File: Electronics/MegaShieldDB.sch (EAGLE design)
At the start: 40 parts, among them IC2 MCP4802, IC3 MCP4802, IC4 4013N, Q1 BF199, Q5 BF199, X1 M25-HD-20, X2 Brake, X4 Cruise Computers, X5 Steer, X6 Motor Controller

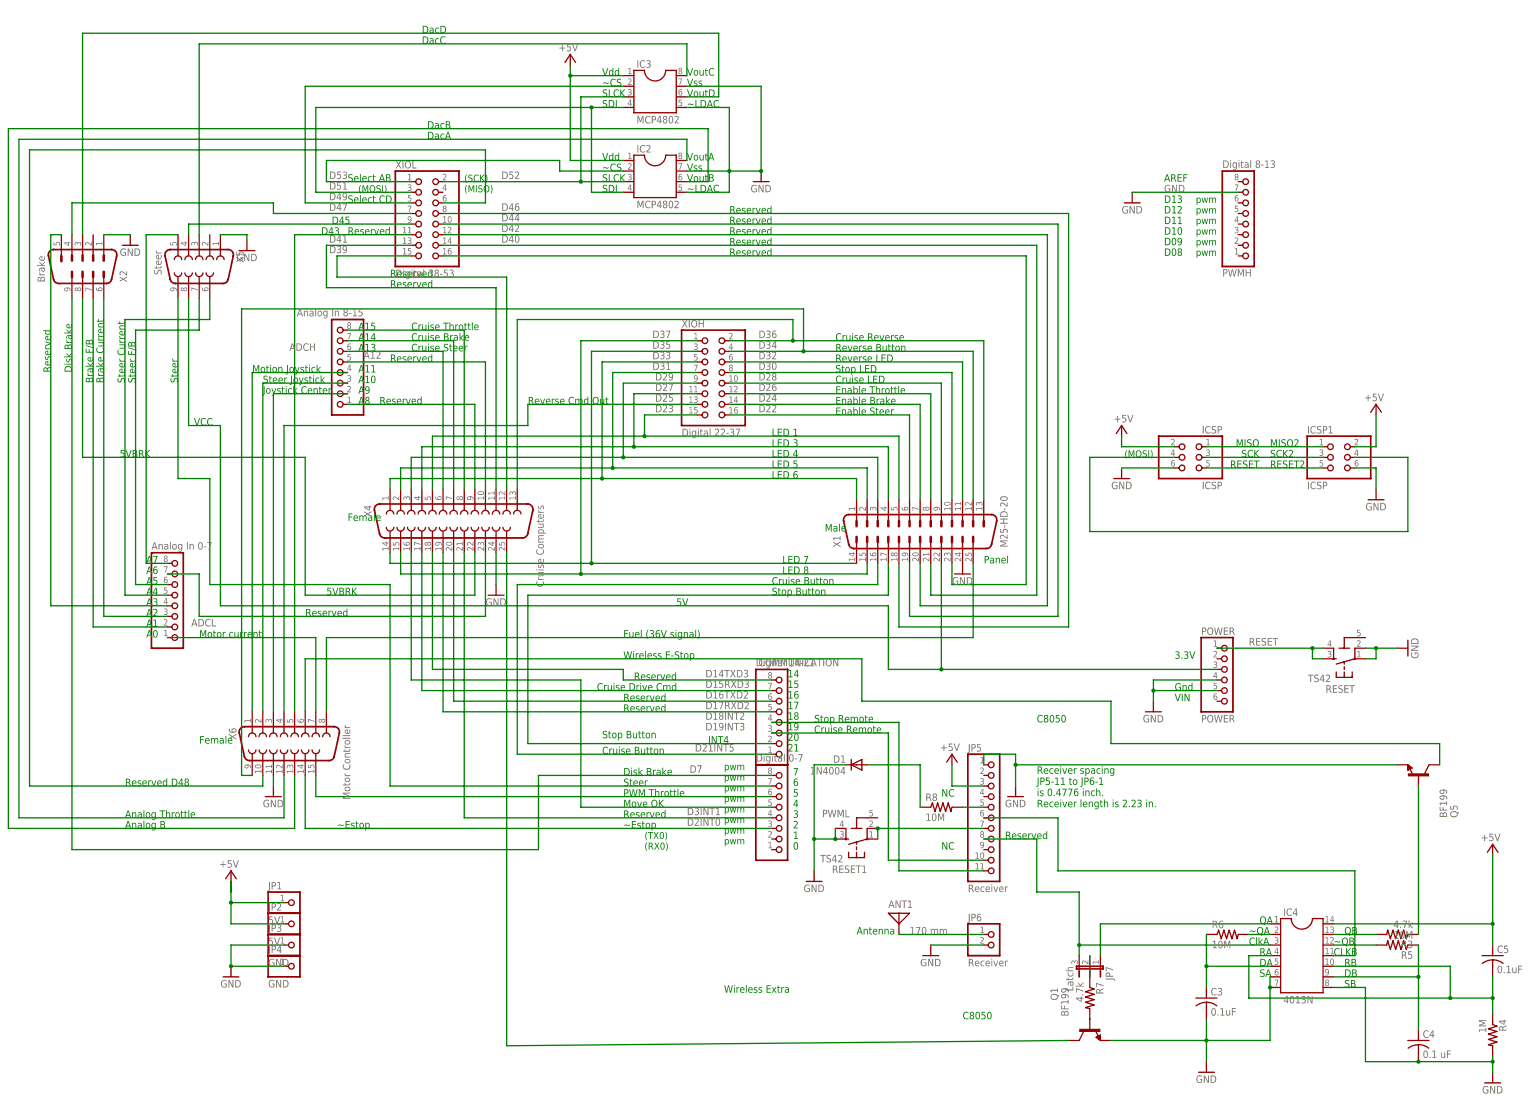
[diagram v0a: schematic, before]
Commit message: Included holes for mounting Mega, board cutouts, renamed connectors. Signals to front panel have been swapped.  Connector names have changed.
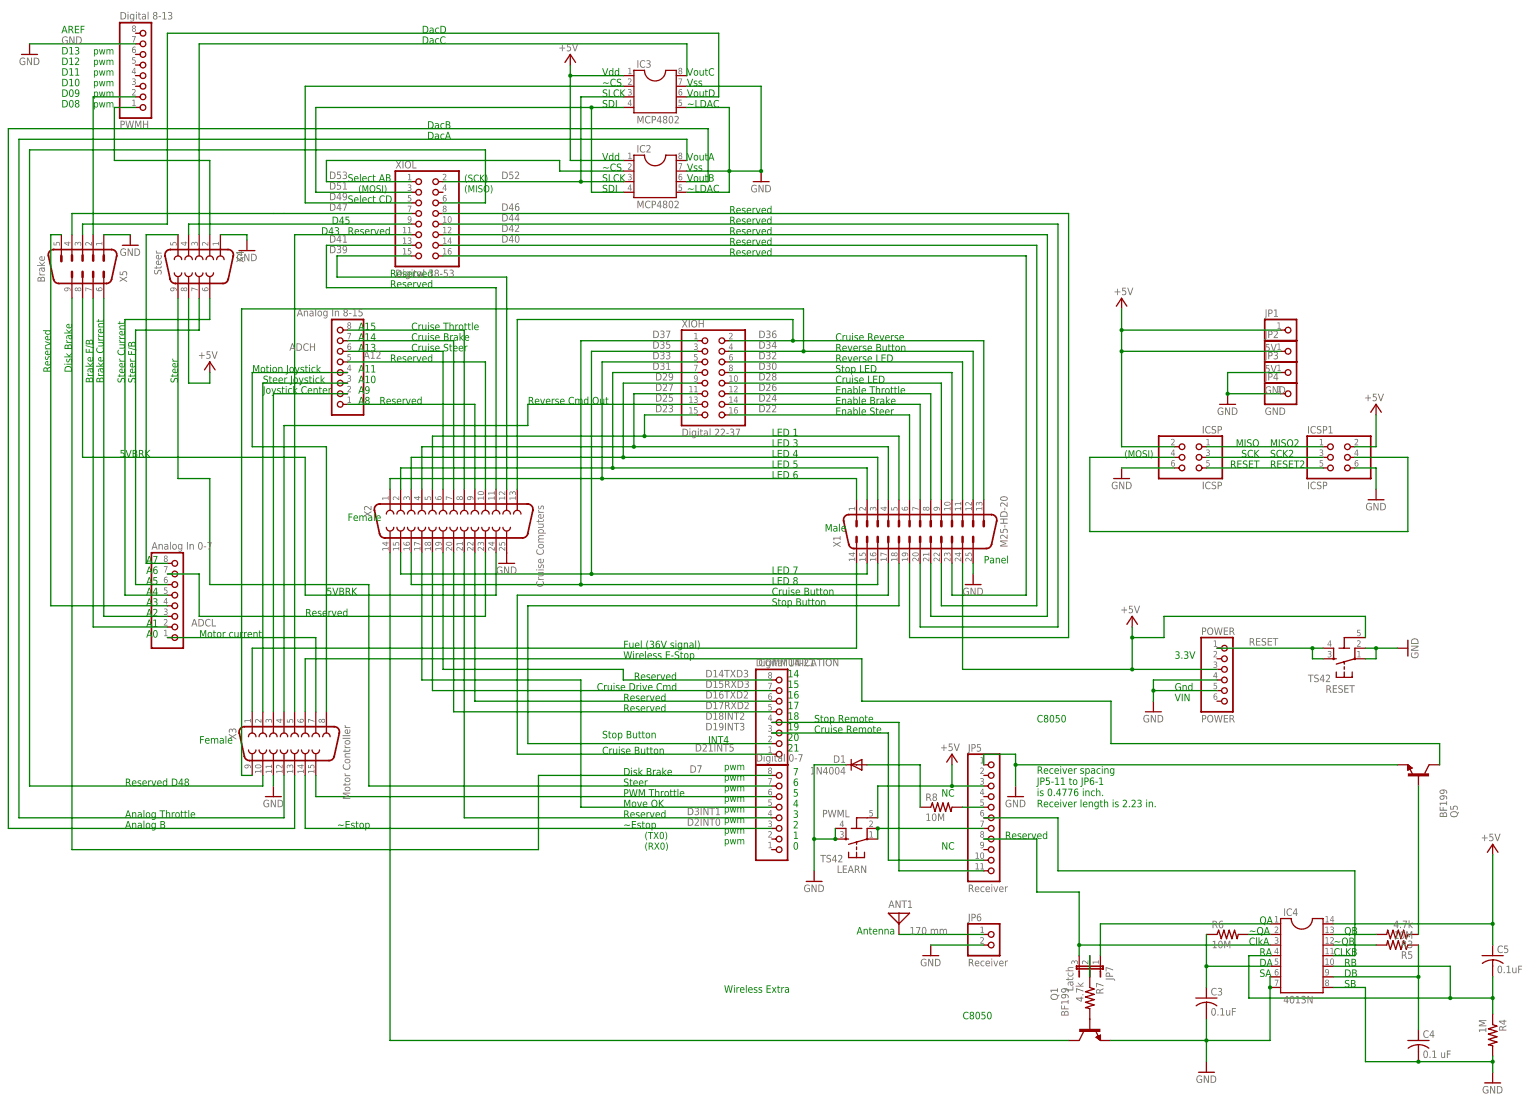
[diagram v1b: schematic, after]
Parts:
- X2: value Brake -> Cruise Computers; device con-subd:M09-182 -> con-subd:F25H
- X4: value Cruise Computers -> Steer; device con-subd:F25H -> con-subd:F09H
- X5: value Steer -> Brake; device con-subd:F09H -> con-subd:M09-182
- renumbered RESET1 to LEARN, X6 to X3
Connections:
- removed net VCC: POWER.3, X1.22, X5.8
- new net N$16: PWMH.2, X5.2
- new net N$17: PWMH.1, X4.2
- net +5V: now also LEARN.5-GND, POWER.3, RESET.5-GND, X1.24, X4.8
- net 5VBRK: now also X2.24, X5.8; no longer X2.8, X4.22
- net A1: now also X5.7; no longer X2.7
- net A11: now also X3.8; no longer X3.1
- net A12: now also X2.10; no longer X4.10
- net A13: now also X2.6; no longer X4.6
- net A14: now also X2.7; no longer X4.7
- net A15: now also X2.8; no longer X4.8
- net A4: now also X4.6; no longer X5.6
- net A5: now also X4.7; no longer X5.7
- net A6: now also X2.23; no longer X4.23
- net A7: now also X4.5; no longer X5.5
- net D14TXD3: now also X2.19; no longer X4.18
- net D15RXD3: now also X2.18; no longer X4.17
- net D16TXD2: now also X2.22; no longer X4.20
- net D17RXD2: now also X2.20; no longer X4.19
- net D20INT4: now also X1.18; no longer X1.17
- net D21INT5: now also X1.17; no longer X1.16
- net D23: now also X2.5; no longer X4.5
- net D27: now also X2.4; no longer X4.4
- net D29: now also X2.3; no longer X4.3
- net D31: now also X2.2; no longer X4.2
- net D33: now also X2.1; no longer X4.1
- net D35: now also X1.15, X2.15; no longer X1.14, X4.14
- net D36: now also X2.13; no longer X4.13
- net D37: now also X1.16, X2.16; no longer X1.15, X4.15
- net D39: now also X2.12; no longer X4.12
- net D3INT1: now also X2.21; no longer X4.21
- net D4: now also X2.17; no longer X4.16
- net D40: now also X1.22; no longer X1.21
- net D41: now also X2.11; no longer X4.11
- net D42: now also X1.21; no longer X1.20
- net D44: now also X1.20; no longer X1.19
- net D45: now also X4.4; no longer X5.4
- net D46: now also X1.19; no longer X1.18
- net D47: now also X5.4; no longer X2.4
- net D6: now also X4.9; no longer X5.9
- net D7: now also X5.9; no longer X2.9
- net DACC: now also X4.3; no longer X5.3
- net DACD: now also X5.3; no longer X2.3
- net FUEL: now also X1.14, X3.1; no longer X1.25, X3.8
- net GND: now also X1.25, X2.25, X4.1; no longer X1.24, X2.1, X4.24
- net N$1: now also X5.6; no longer X2.6
- net N$5: now also X2.9; no longer X4.9
- net N$8: now also X5.5; no longer X2.5
- net WLX: now also X2.14; no longer X4.25
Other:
- note removed: "5V"
- note removed: "VCC"
- moved on the sheet: JP1, JP2, JP3, JP4, PWMH

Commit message: Mirrored Arduino pins for bottom mount. Added Wheel Revolution with pull-up resistor.
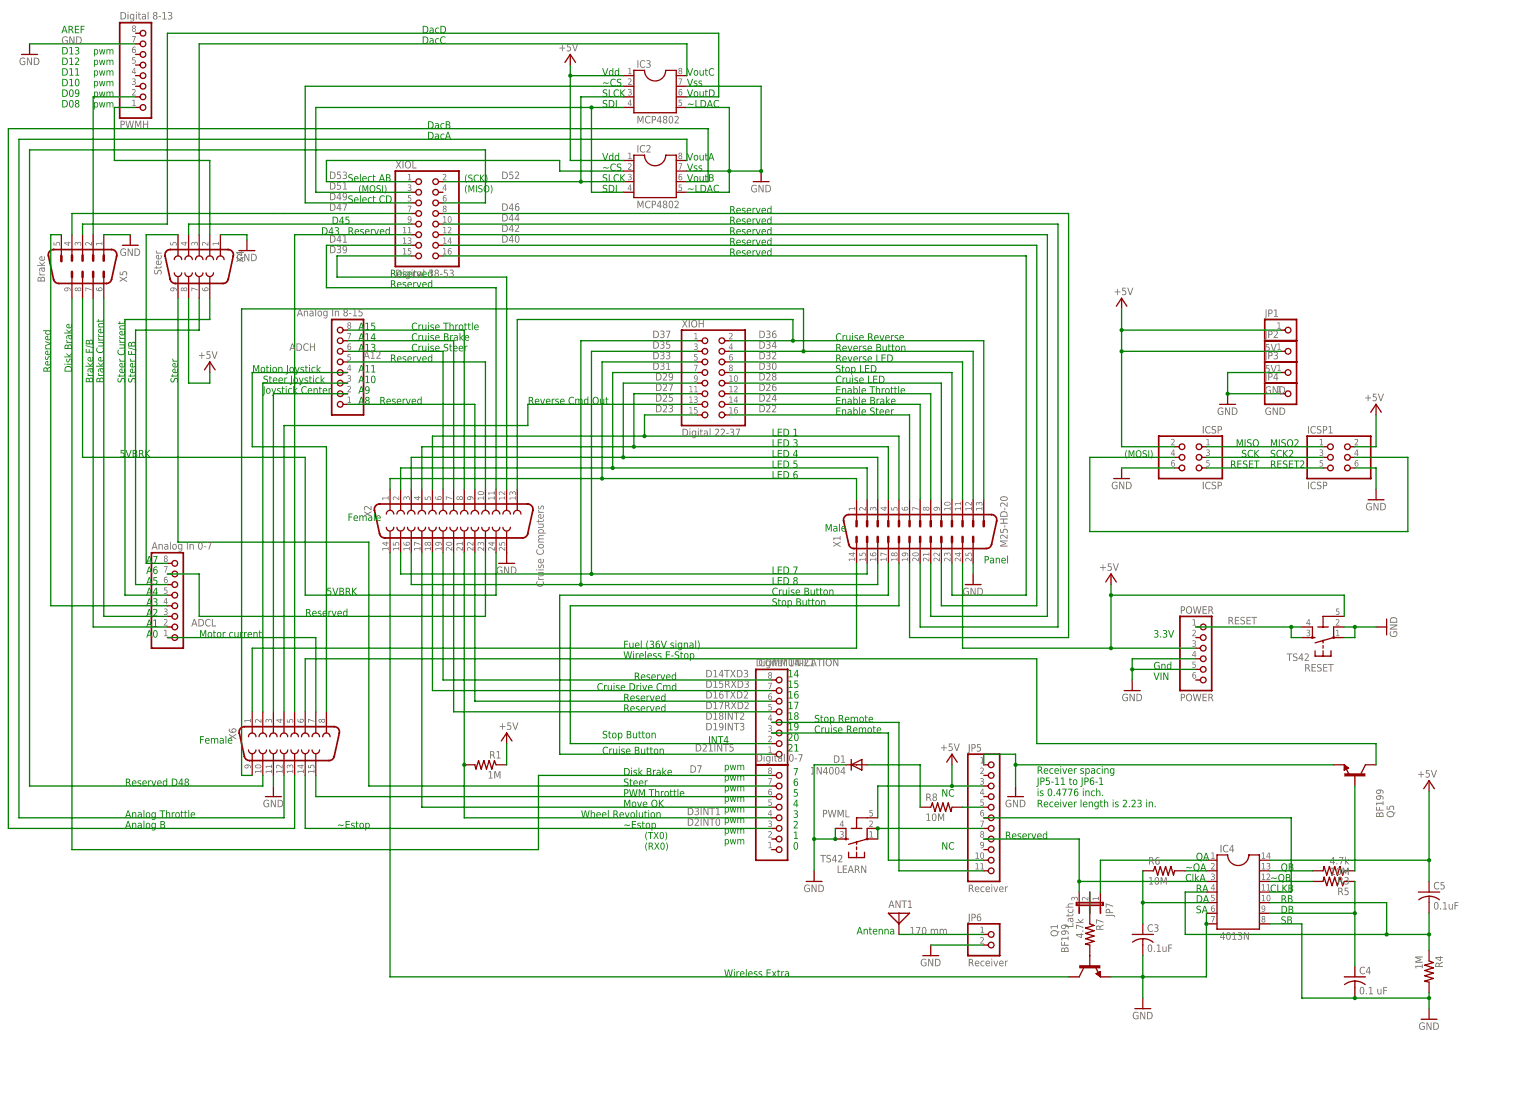
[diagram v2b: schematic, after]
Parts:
- removed X3: Motor Controller, con-subd:F15HP
- added R1: 1M, rcl:R-US_0204/5
- added X6: (no value), con-subd:F15H
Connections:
- net N$16 renamed D9
- net N$17 renamed D8
- net +5V: now also R1.1
- net A0: now also X6.7; no longer X3.7
- net A10: now also X6.2; no longer X3.2
- net A11: now also X6.8; no longer X3.8
- net A9: now also X6.3; no longer X3.3
- net D25: now also X6.4; no longer X3.4
- net D2INT0: now also X6.14; no longer X3.14
- net D34: now also X6.9; no longer X3.9
- net D3INT1: now also R1.2
- net D43: now also X6.5; no longer X3.5
- net D48: now also X6.10; no longer X3.10
- net D5: now also X6.15; no longer X3.15
- net DACA: now also X6.12; no longer X3.12
- net DACB: now also X6.13; no longer X3.13
- net FUEL: now also X6.1; no longer X3.1
- net GND: now also X6.11; no longer X3.11
- net WLES: now also X6.6; no longer X3.6
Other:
- note added: "Wheel Revolution"
- note removed: "C8050"
- moved on the sheet: C3, C4, C5, IC4, JP7, POWER, Q1, Q5, R3, R4, R5, R6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

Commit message: Rearranged jumper.
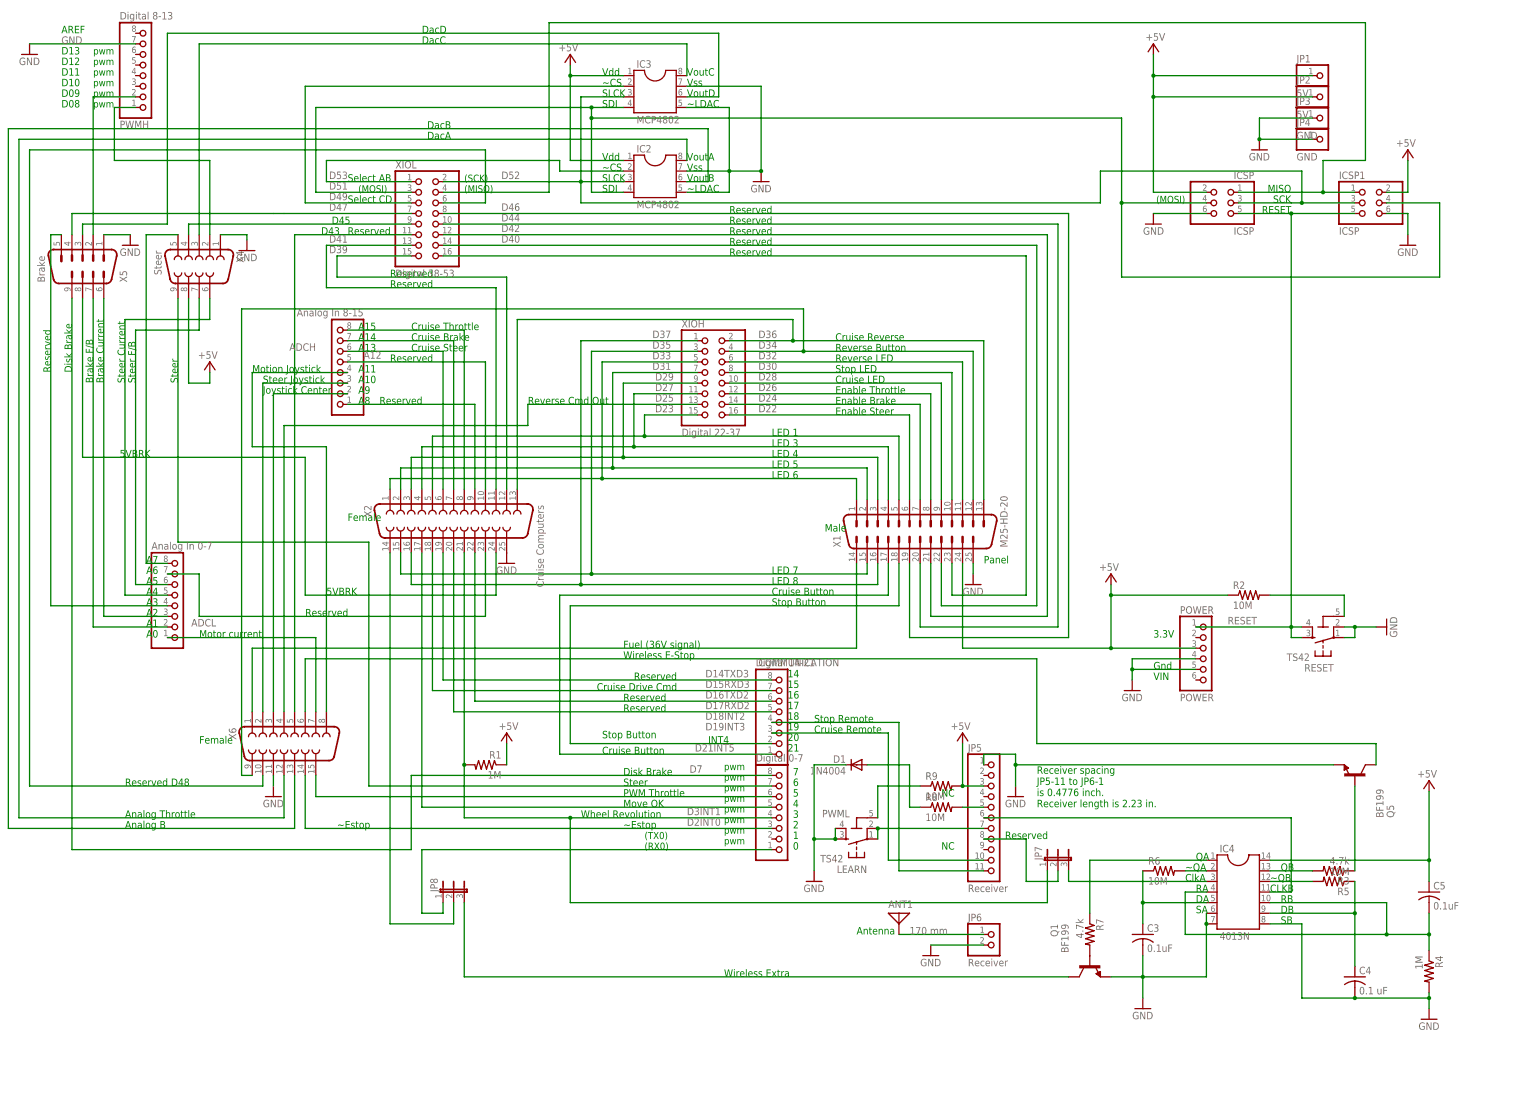
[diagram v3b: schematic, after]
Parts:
- added JP8: (no value), jumper:JP2E
- added R2, R9: 10M, rcl:R-US_0204/5
- JP7: value Latch -> (none)
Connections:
- net N$3 renamed RCVR5
- removed net N$11: JP7.2, R7.1
- removed net N$13: ICSP.5, ICSP1.5
- removed net N$14: ICSP.4, ICSP1.4
- removed net WLX: Q1.C, X2.14
- new net D0RX0: JP8.1, PWML.1
- new net N$6: R2.2, RESET.5-GND
- new net WL2: JP5.8, JP7.2
- new net WLXCOLL: JP8.3, Q1.C
- new net X2-14: JP8.2, X2.14
- net +5V: now also R2.1, R9.2; no longer LEARN.5-GND, RESET.5-GND
- net CLKA: no longer JP5.8
- net D3INT1: now also JP7.1
- net D51: now also ICSP.4, ICSP1.4
- net D52: now also ICSP.3, ICSP1.3
- net N$10: now also LEARN.5-GND, R9.1; no longer ICSP.3, ICSP1.3
- net N$2: now also R7.1; no longer JP7.1
- net N$9: now also XIOL.4
- net RESET: now also ICSP.5, ICSP1.5
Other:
- note removed: "MISO2"
- note removed: "RESET2"
- note removed: "SCK2"
- moved on the sheet: ICSP, ICSP1, JP1, JP2, JP3, JP4, JP7

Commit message: update to Sourceforge 123
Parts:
- removed JP7, JP8: (no value), jumper:JP2E
- removed LEARN, RESET: TS42, st-mod v1.4:TS42
- removed X6: (no value), con-subd:F15H
- added JP9: (no value), jumper:JP3Q
- added LSP1, LSP2: LSP13, solpad:LSP13
- added U$1, U$2: DPDT_DEV6X5MM_PAC, elcanoParts:DPDT_DEV6X5MM_PAC
- added X3: Motor, con-subd:M15-182
- X1: value M25-HD-20 -> Panel
- X2: value Cruise Computers -> Cruise
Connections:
- net A0: now also X3.7; no longer X6.7
- net A10: now also X3.2; no longer X6.2
- net A11: now also X3.8; no longer X6.8
- net A9: now also X3.3; no longer X6.3
- net CLKA: now also JP9.6; no longer JP7.3
- net D0RX0: now also JP9.1; no longer JP8.1
- net D25: now also X3.4; no longer X6.4
- net D2INT0: now also X3.14; no longer X6.14
- net D34: now also X3.9; no longer X6.9
- net D3INT1: now also JP9.2; no longer JP7.1
- net D43: now also X3.5; no longer X6.5
- net D48: now also X3.10; no longer X6.10
- net D5: now also X3.15; no longer X6.15
- net DACA: now also X3.12; no longer X6.12
- net DACB: now also X3.13; no longer X6.13
- net FUEL: now also X3.1; no longer X6.1
- net GND: now also U$1.3, U$1.6, U$2.3, U$2.6, X3.11; no longer LEARN.3, LEARN.4, RESET.1, RESET.2, X6.11
- net N$10: now also U$2.1, U$2.4; no longer LEARN.5-GND
- net N$28: now also U$2.2, U$2.5; no longer LEARN.1, LEARN.2
- net N$6: now also U$1.1, U$1.4; no longer RESET.5-GND
- net RESET: now also U$1.2, U$1.5; no longer RESET.3, RESET.4
- net WL2: now also JP9.4; no longer JP7.2
- net WLES: now also X3.6; no longer X6.6
- net WLXCOLL: now also JP9.5; no longer JP8.3
- net X2-14: now also JP9.3; no longer JP8.2
